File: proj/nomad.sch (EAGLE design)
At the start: 20 parts, among them P7 5.5V-VUSB-GND, P8 5.5V-BOOST_IN-GND, U2 TPS61200S-PVSON-N10, U3 MAX1811SO8

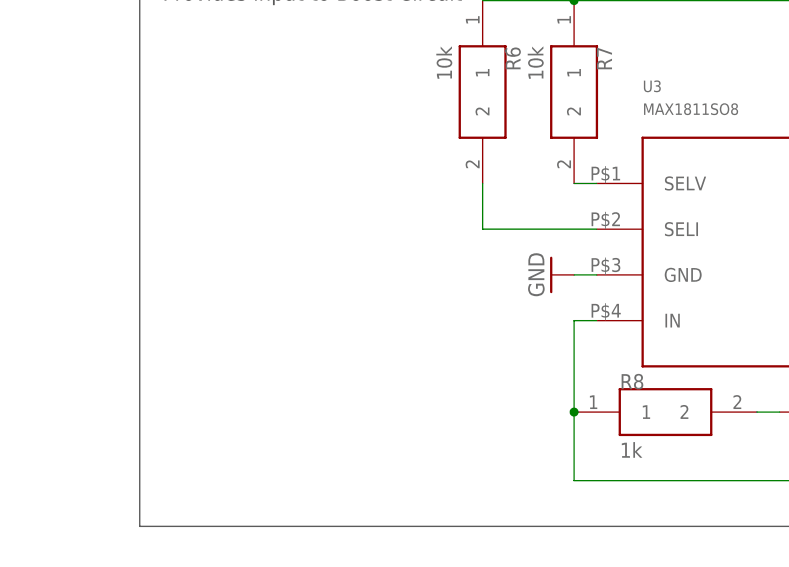
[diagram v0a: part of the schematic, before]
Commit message: Added Solder Jumper to Nomad module to select charge current (open = 500mA / closed = 100mA) @open #13 @close #13
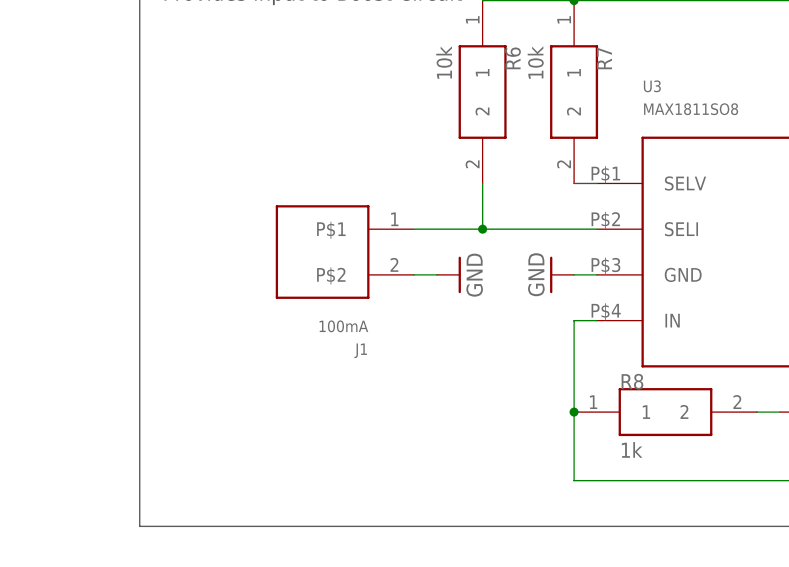
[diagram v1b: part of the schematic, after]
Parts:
- added J1: 100mA, dooba:JMPSMD
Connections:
- net GND: now also J1.P$2
- net N$20: now also J1.P$1
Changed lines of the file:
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@@
 <?xml version="1.0" encoding="utf-8"?>
 <!DOCTYPE eagle SYSTEM "eagle.dtd">
-<eagle version="7.7.0">
+<eagle version="7.3.0">
 <drawing>
 <settings>
@@
 <layer number="115" name="ReferenceISLANDS" color="7" fill="1" visible="yes" active="yes"/>
 <layer number="116" name="Patch_BOT" color="9" fill="4" visible="yes" active="yes"/>
+<layer number="117" name="Refs" color="11" fill="1" visible="yes" active="yes"/>
 <layer number="118" name="Rect_Pads" color="7" fill="1" visible="yes" active="yes"/>
 <layer number="121" name="_tsilk" color="7" fill="1" visible="yes" active="yes"/>
@@
 <part name="BATT(VCC-GND)1" library="dooba" deviceset="PIN_2" device="" value="VBAT-GND"/>
 <part name="GND1" library="supply1" deviceset="GND" device=""/>
+<part name="J1" library="dooba" deviceset="JMP" device="SMD" value="100mA"/>
+<part name="GND2" library="supply1" deviceset="GND" device=""/>
 </parts>
 <sheets>
@@
 <instance part="BATT(VCC-GND)1" gate="P1" x="139.7" y="139.7" rot="MR90"/>
 <instance part="GND1" gate="1" x="137.16" y="127"/>
+<instance part="J1" gate="J1" x="43.18" y="144.78" rot="R180"/>
+<instance part="GND2" gate="1" x="58.42" y="142.24" rot="R90"/>
 </instances>
 <busses>
@@
 <pinref part="GND1" gate="1" pin="GND"/>
 <wire x1="137.16" y1="132.08" x2="137.16" y2="129.54" width="0.1524" layer="91"/>
+</segment>
+<segment>
+<pinref part="J1" gate="J1" pin="P$2"/>
+<pinref part="GND2" gate="1" pin="GND"/>
+<wire x1="55.88" y1="142.24" x2="53.34" y2="142.24" width="0.1524" layer="91"/>
 </segment>
 </net>
@@
 <wire x1="73.66" y1="147.32" x2="60.96" y2="147.32" width="0.1524" layer="91"/>
 <wire x1="60.96" y1="147.32" x2="60.96" y2="152.4" width="0.1524" layer="91"/>
-</segment>
-</net>
+<pinref part="J1" gate="J1" pin="P$1"/>
+<wire x1="53.34" y1="147.32" x2="60.96" y2="147.32" width="0.1524" layer="91"/>
+<junction x="60.96" y="147.32"/>
+</segment>
+</net>

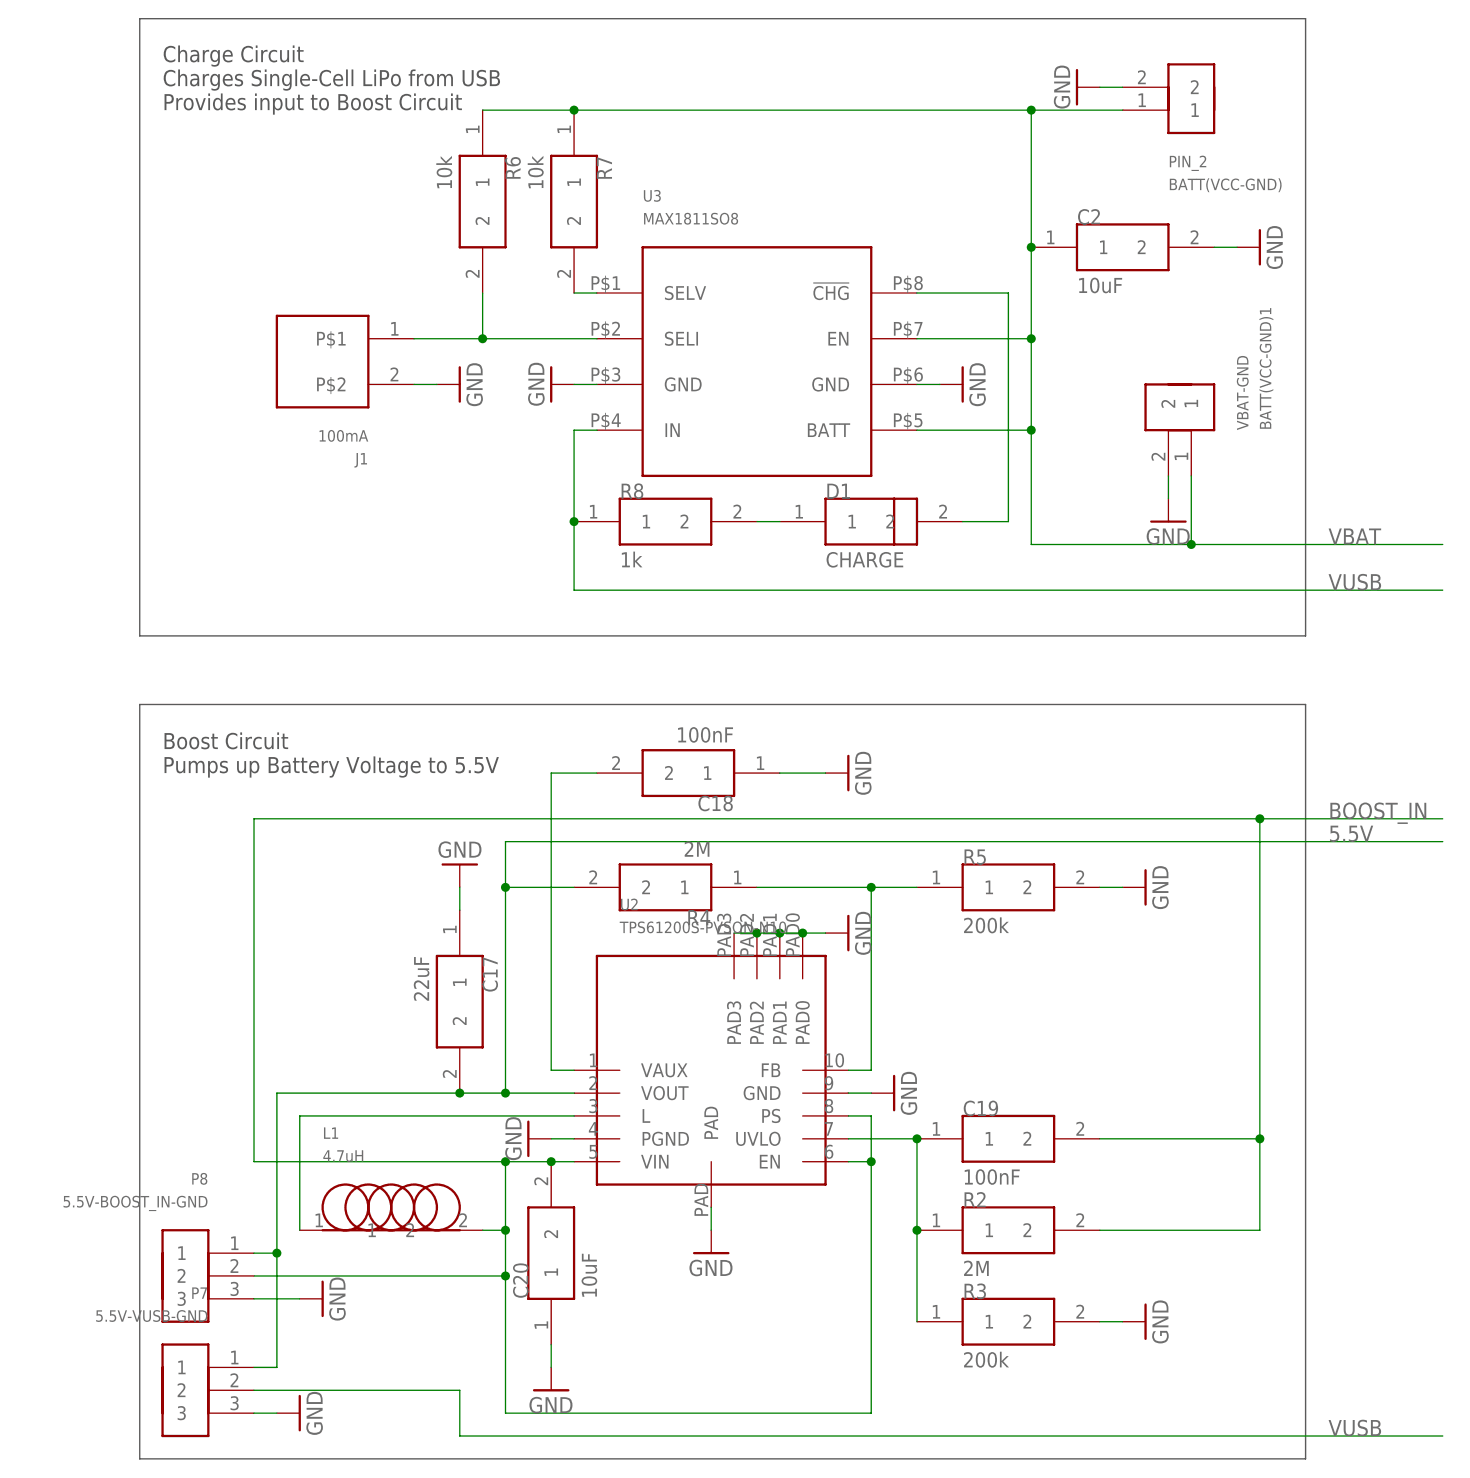
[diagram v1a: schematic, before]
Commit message: Completed new Shiva board using SPI for MicroSD and Aecho Improved some QFN parts in the Eagle Library Added ref layer to Nomad for ZFPCBA @close #7
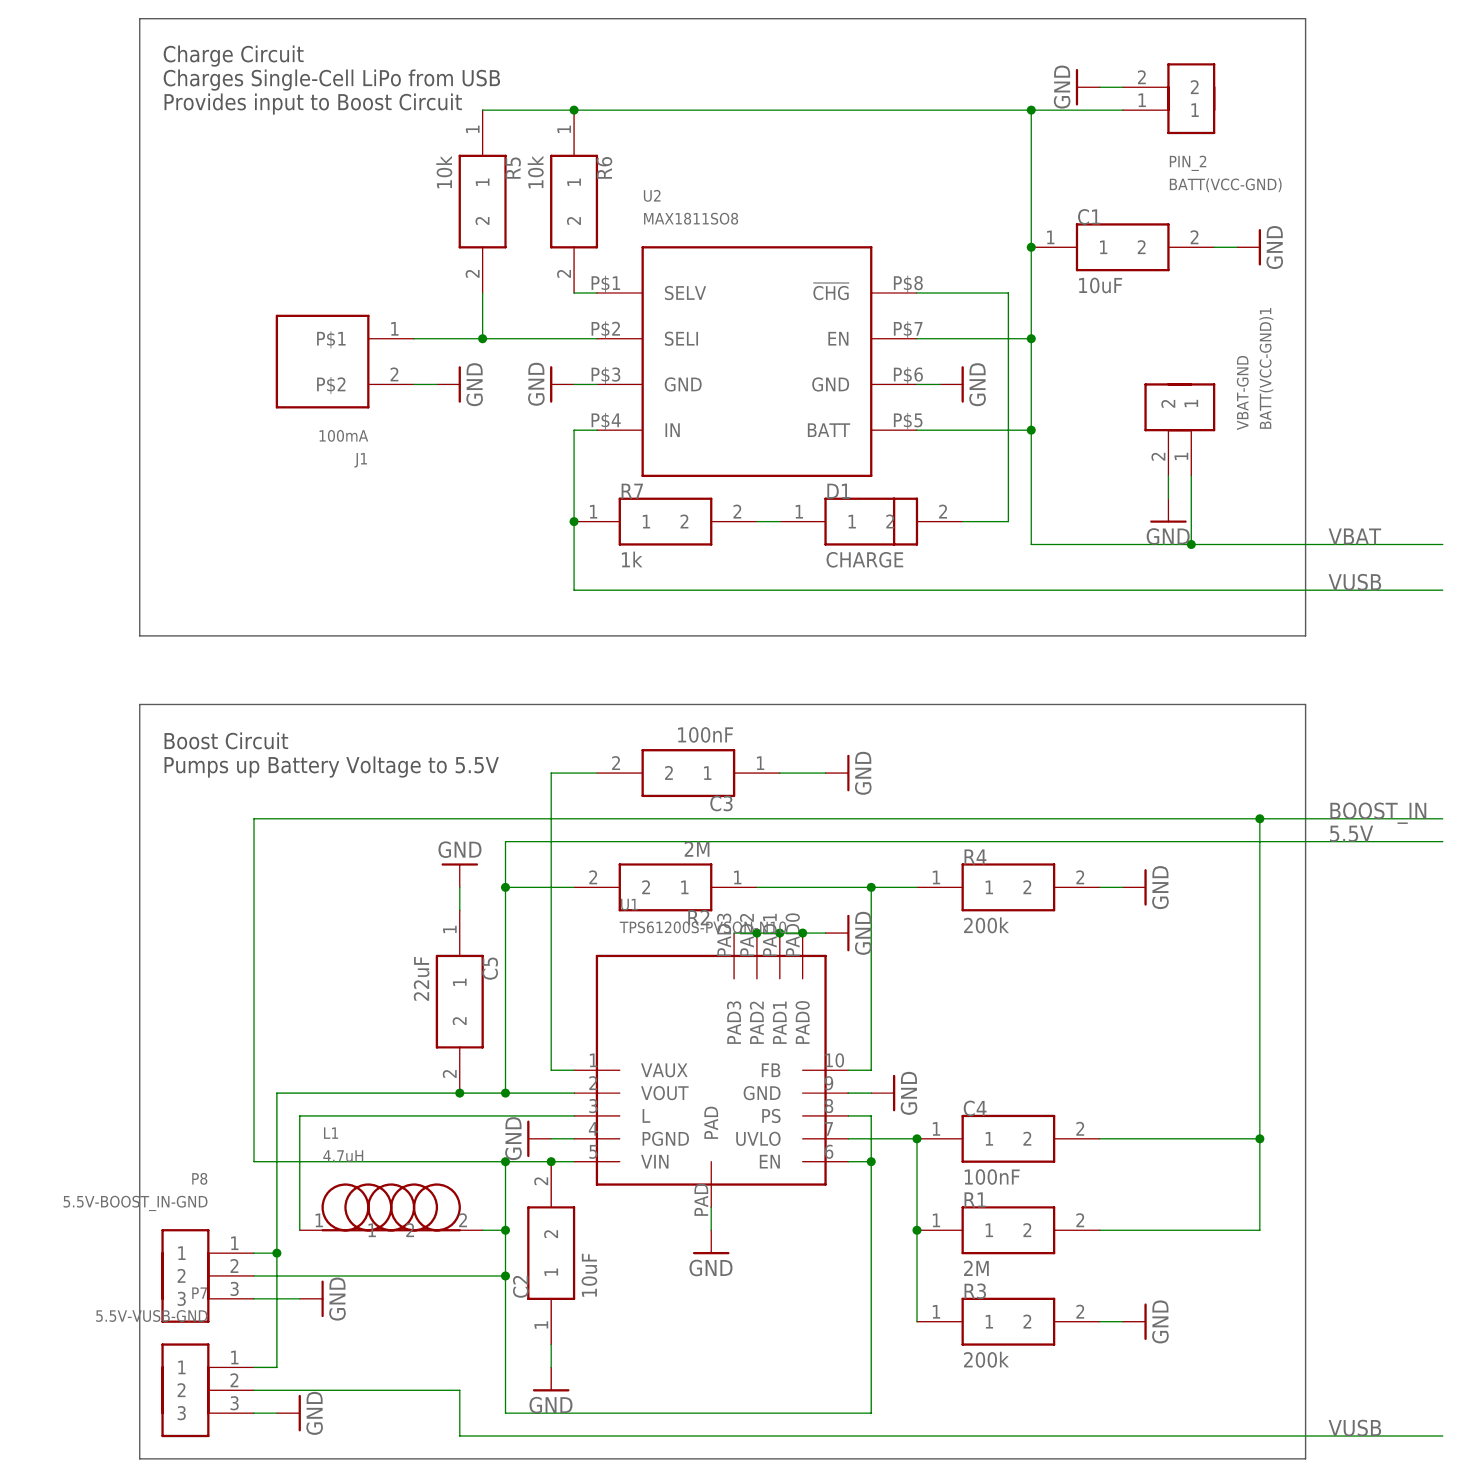
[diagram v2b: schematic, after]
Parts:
- removed C20: 10uF, dooba:CAP0805
- removed R8: 1k, dooba:RES0805
- removed U3: MAX1811SO8, dooba:MAX1811SO8
- added C1: 10uF, dooba:CAP0805
- added R1: 2M, dooba:RES0805
- added U1: TPS61200S-PVSON-N10, dooba:TPS61200S-PVSON-N10
- R4: value 2M -> 200k
- R5: value 200k -> 10k
- R7: value 10k -> 1k
- U2: value TPS61200S-PVSON-N10 -> MAX1811SO8; device dooba:TPS61200S-PVSON-N10 -> dooba:MAX1811SO8
- renumbered C17 to C5, C18 to C3, C19 to C4
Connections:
- net 5.5V: now also R2.2, U1.VOUT; no longer R4.2, U2.VOUT
- net BOOST_IN: now also C2.2, R1.2, U1.EN, U1.PS, U1.VIN; no longer C20.2, R2.2, U2.EN, U2.PS, U2.VIN
- net GND: now also C1.2, C2.1, R4.2, U1.GND, U1.PAD, U1.PAD0, U1.PAD1, U1.PAD2, U1.PAD3, U1.PGND, U2.GND@3, U2.GND@6; no longer C2.2, C20.1, R5.2, U2.GND, U2.PAD, U2.PAD0, U2.PAD1, U2.PAD2, U2.PAD3, U2.PGND, U3.GND@3, U3.GND@6
- net N$13: now also R1.1, U1.UVLO; no longer R2.1, U2.UVLO
- net N$14: now also R2.1, U1.FB; no longer R5.1, U2.FB
- net N$15: now also U1.VAUX; no longer U2.VAUX
- net N$16: now also U1.L; no longer U2.L
- net N$17: now also U2.!CHG; no longer U3.!CHG
- net N$18: now also R7.2; no longer R8.2
- net N$19: now also R6.2, U2.SELV; no longer R7.2, U3.SELV
- net N$20: now also R5.2, U2.SELI; no longer R6.2, U3.SELI
- net VBAT: now also C1.1, R5.1, U2.BATT, U2.EN; no longer C2.1, R7.1, U3.BATT, U3.EN
- net VUSB: now also R7.1, U2.IN; no longer R8.1, U3.IN
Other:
- moved on the sheet: C2, R2, R4, R5, R6, R7
